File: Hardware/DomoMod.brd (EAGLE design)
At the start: 80 x 30 mm, 47 parts, among them Q1 BSS138, Q2 BSS138, T1 MMBT2222A, U1 NCS36000, U2 CCS811, U3 BME280, U4 PIR

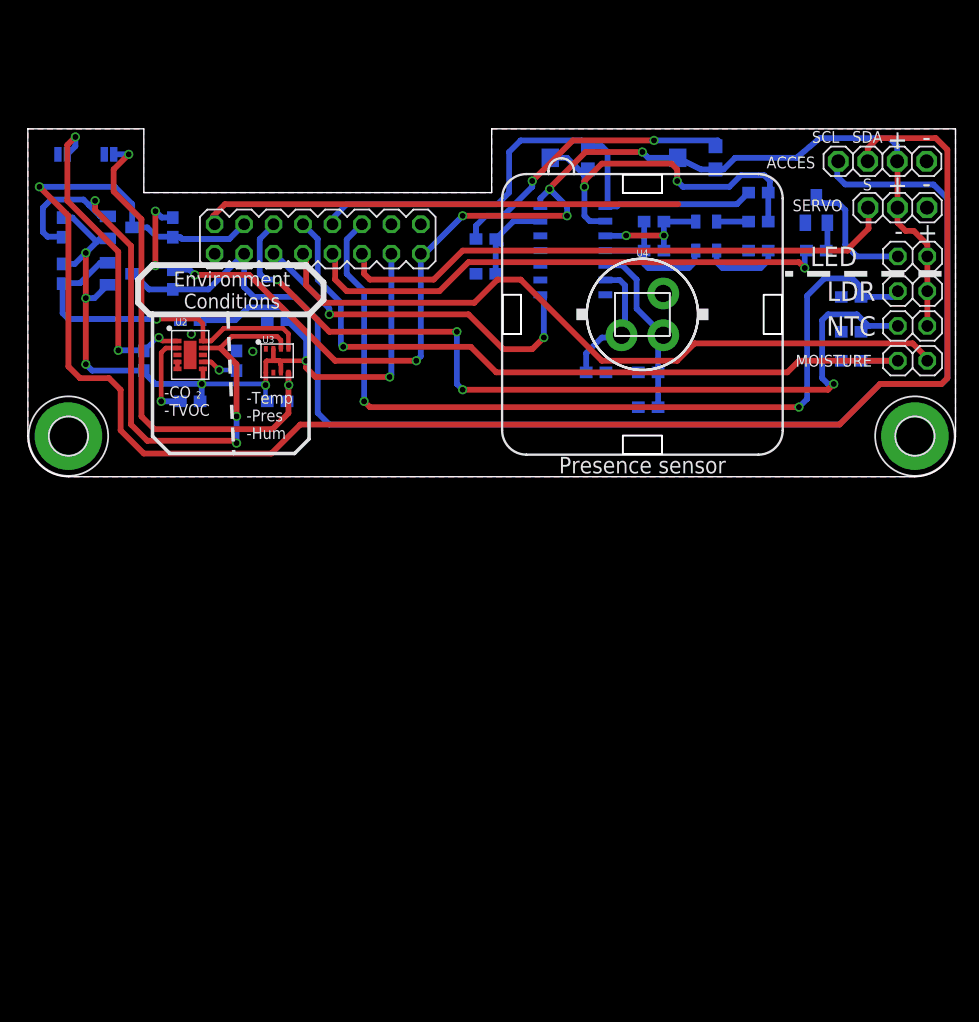
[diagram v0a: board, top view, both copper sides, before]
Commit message: Component replacement: NCS36000 -> BD9251FV
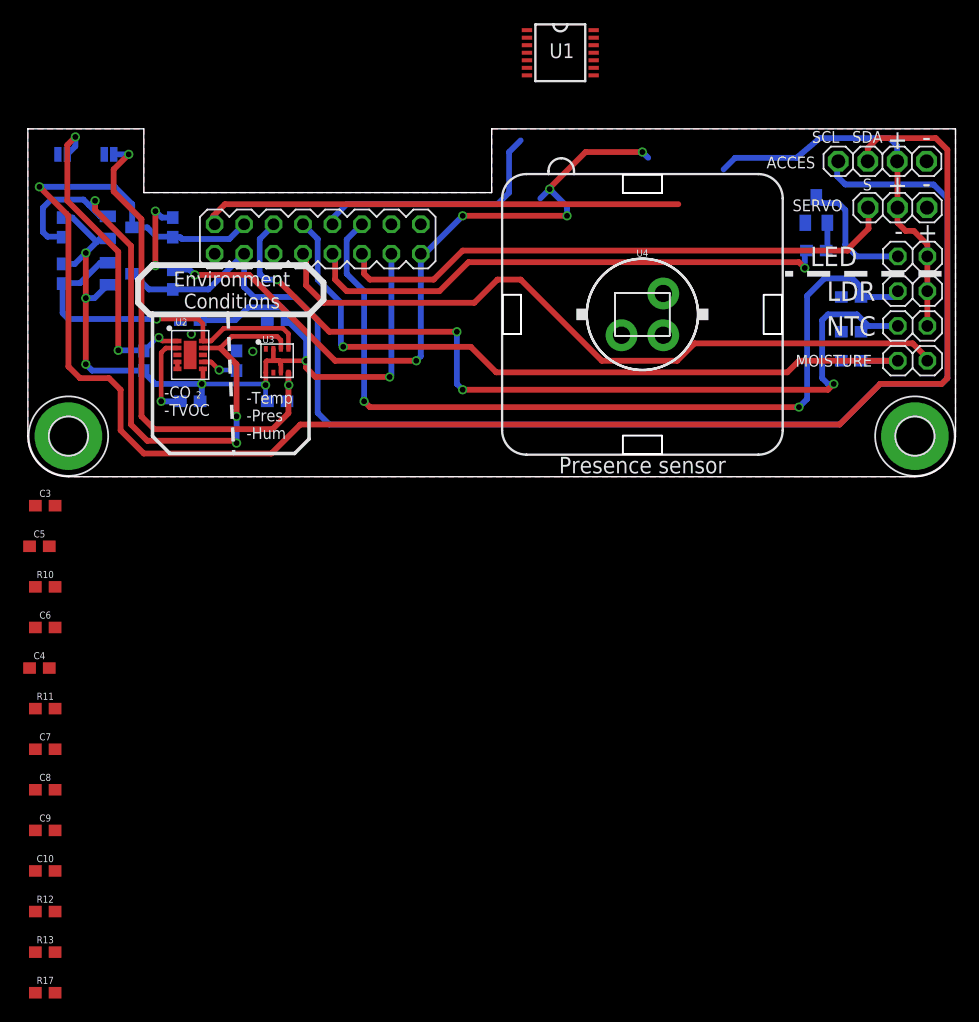
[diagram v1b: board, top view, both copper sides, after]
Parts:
- removed POT1, POT2: 1M, openPIR-temp:TRIMPOT-TC33X
- added C10: 10uF, SparkFun-Capacitors:0603
- C3: value 22uF -> 1.0uF; device SparkFun-Capacitors:0805 -> SparkFun-Capacitors:0603
- C4: value 10nF -> 1.0uF
- C5: value 0.1uF -> 1.0uF
- C6: value 0.1uF -> 6.9uF
- C7: value 22uF -> 15nF; device SparkFun-Capacitors:0805 -> SparkFun-Capacitors:0603
- C8: value 10nF -> 6.9uF
- C9: value 0.1uF -> 15nF
- R10: value 10k -> 47k
- R11: value 10k -> 4.7M
- R12: value 43k -> 47k
- R13: value 51k -> 4.7M; device openPIR-temp:0603 -> SparkFun-Resistors:0603
- R17: value 560k -> 220k; device openPIR-temp:0603 -> SparkFun-Resistors:0603
- U1: value NCS36000 -> BD9251FV; device openPIR-temp:SO14 -> SpaceDIY_IC:TSSOP-14
- moved R17 84.7 mm to (1.50, -44.5), flipped to the top, turned to 0 degrees
- moved C8 80.2 mm to (1.50, -27.0), flipped to the top
- moved R11 74.5 mm to (1.50, -20.0), flipped to the top, turned to 0 degrees
- moved C7 72.9 mm to (1.50, -23.5), flipped to the top, turned to 0 degrees
- moved R13 72.3 mm to (1.50, -41.0), flipped to the top
- moved R10 68.0 mm to (1.50, -9.50), flipped to the top, turned to 0 degrees
- moved R12 67.8 mm to (1.50, -37.5), flipped to the top, turned to 0 degrees
- moved C4 64.1 mm to (1.00, -16.5), flipped to the top, turned to 0 degrees
- moved C9 61.2 mm to (1.50, -30.5), flipped to the top
- moved C3 61.1 mm to (1.50, -2.50), flipped to the top, turned to 0 degrees
- moved C5 54.6 mm to (1.00, -6.00), flipped to the top
- moved C6 52.3 mm to (1.50, -13.0), flipped to the top, turned to 0 degrees
- moved U1 17.0 mm to (46.0, 36.5), flipped to the top, turned to 0 degrees
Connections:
- removed net N$11: POT2.1, R13.2
- removed net N$3: C3.2, R10.2
- removed net N$4: C7.2, R11.1
- removed net N$6: C4.2, C7.1, R17.2, U1.3
- removed net N$7: C8.1, POT1.2, POT1.3, R11.2, U1.2
- removed net N$8: C9.1, R13.1, U1.13
- new net A1N: C7.2, R10.1, R11.2, U1.5
- new net A1O: C7.1, C8.2, R11.1, U1.6
- new net A2N: C9.2, R12.1, R13.2, U1.8
- new net A2O: C10.1, C9.1, R13.1, U1.9
- new net A2P: C8.1, R12.2, U1.7
- new net COMP: C10.2, R17.2, U1.11
- new net OUT: U1.12
- new net REF: R17.1, U1.10
- net A2: no longer C8.2, POT1.1, U1.1
- net D8: no longer U1.8
- net GND: now also C3.2, C4.2, U1.1; no longer C9.2, R10.1, R12.1, U1.7
- net N$1: now also C6.1, R10.2; no longer C5.1, R12.2, U1.5, U4.S
- net N$2: now also C3.1, U1.4, U4.S; no longer C6.1, U1.6, U4.D
- net N$5: now also U1.3, U4.D; no longer C3.1, R17.1, U1.4
- net VCC: now also C5.1; no longer POT2.2, POT2.3
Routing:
- net N$7: track 32.4 -> 0.00 mm, vias 2 -> 0
- net D8: track 31.2 -> 0.00 mm, vias 2 -> 0
- net N$11: track 26.0 -> 0.00 mm, vias 2 -> 0
- net A2: track 47.1 -> 21.6 mm
- net N$1: track 15.3 -> 0.00 mm
- net N$5: track 12.7 -> 0.00 mm
- net N$2: track 11.7 -> 0.00 mm
- net N$6: track 10.3 -> 0.00 mm, vias 2 -> 0
- net N$8: track 8.14 -> 0.00 mm
- net VCC: track 110.7 -> 103.3 mm
- net N$3: track 6.78 -> 0.00 mm
- net N$4: track 2.75 -> 0.00 mm

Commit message: BRD and Production files updated for component BD9251FV
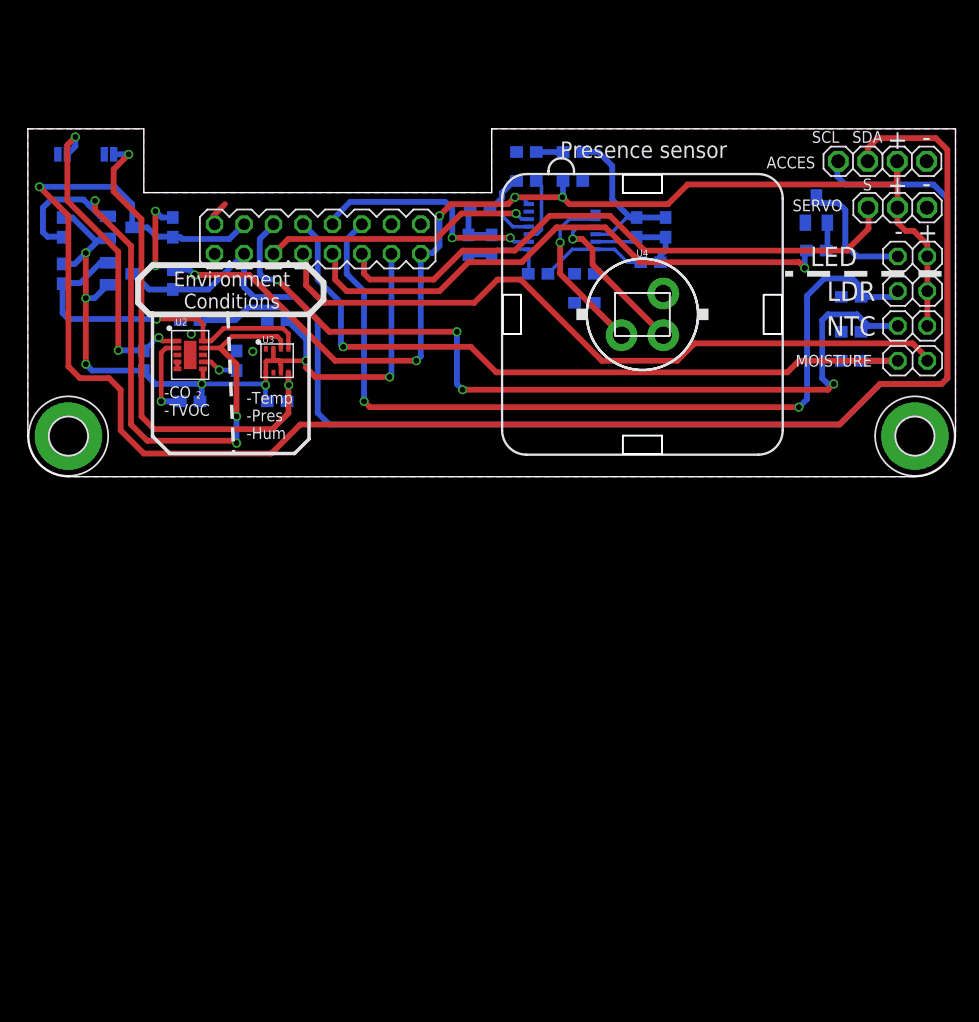
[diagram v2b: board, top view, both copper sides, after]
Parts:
- moved R17 81.4 mm to (43.0, 25.5), flipped to the bottom
- moved R13 71.1 mm to (38.0, 20.0), flipped to the bottom, turned to 270 degrees
- moved C7 69.9 mm to (55.0, 21.5), flipped to the bottom, turned to 90 degrees
- moved R12 69.5 mm to (44.0, 17.5), flipped to the bottom, turned to 180 degrees
- moved C8 69.2 mm to (53.7, 18.5), flipped to the bottom, turned to 180 degrees
- moved C10 68.2 mm to (39.0, 23.0), flipped to the bottom, turned to 180 degrees
- moved R11 65.8 mm to (52.5, 21.5), flipped to the bottom, turned to 90 degrees
- moved C9 63.5 mm to (40.0, 20.0), flipped to the bottom, turned to 270 degrees
- moved R10 59.0 mm to (47.0, 28.0), flipped to the bottom
- moved C6 58.3 mm to (43.0, 28.0), flipped to the bottom
- moved C4 56.6 mm to (48.0, 15.0), flipped to the bottom
- moved C5 55.8 mm to (47.0, 25.5), flipped to the bottom, turned to 180 degrees
- moved C3 50.6 mm to (48.0, 17.5), flipped to the bottom
- moved U1 15.0 mm to (46.0, 21.5), flipped to the bottom
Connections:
- removed net OUT: U1.12
- net A2: now also U1.9
- net A2O: no longer U1.9
- net D8: now also U1.12
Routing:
- net D0: track 41.3 -> 2.19 mm
- net D8: track 0.00 -> 23.7 mm, vias 0 -> 1
- net N$2: track 0.00 -> 22.9 mm, vias 0 -> 1
- net N$5: track 0.00 -> 18.6 mm, vias 0 -> 1
- net A1N: track 0.00 -> 14.9 mm
- net A2P: track 0.00 -> 9.33 mm
- net A1O: track 0.00 -> 8.54 mm
- net COMP: track 0.00 -> 7.55 mm
- net A2N: track 0.00 -> 7.53 mm
- net REF: track 0.00 -> 5.64 mm
- net VCC: track 103.3 -> 107.7 mm, vias 8 -> 7
- net A2O: track 0.00 -> 4.21 mm
- net D6: track 46.0 -> 48.5 mm
- net D5: track 49.3 -> 51.8 mm
- net N$1: track 0.00 -> 2.30 mm
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
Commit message: Added Schematics.pdf
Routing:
- net D0: track 2.19 -> 0.00 mm
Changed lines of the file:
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@@
 <signal name="D0">
 <contactref element="SV1" pad="2"/>
-<wire x1="17" y1="23.5" x2="16" y2="22.5" width="0.5" layer="1"/>
-<wire x1="16" y1="22.5" x2="16" y2="21.88" width="0.5" layer="1"/>
-<wire x1="16" y1="21.88" x2="16.11" y2="21.77" width="0.5" layer="1"/>
 </signal>
 <signal name="!RST">

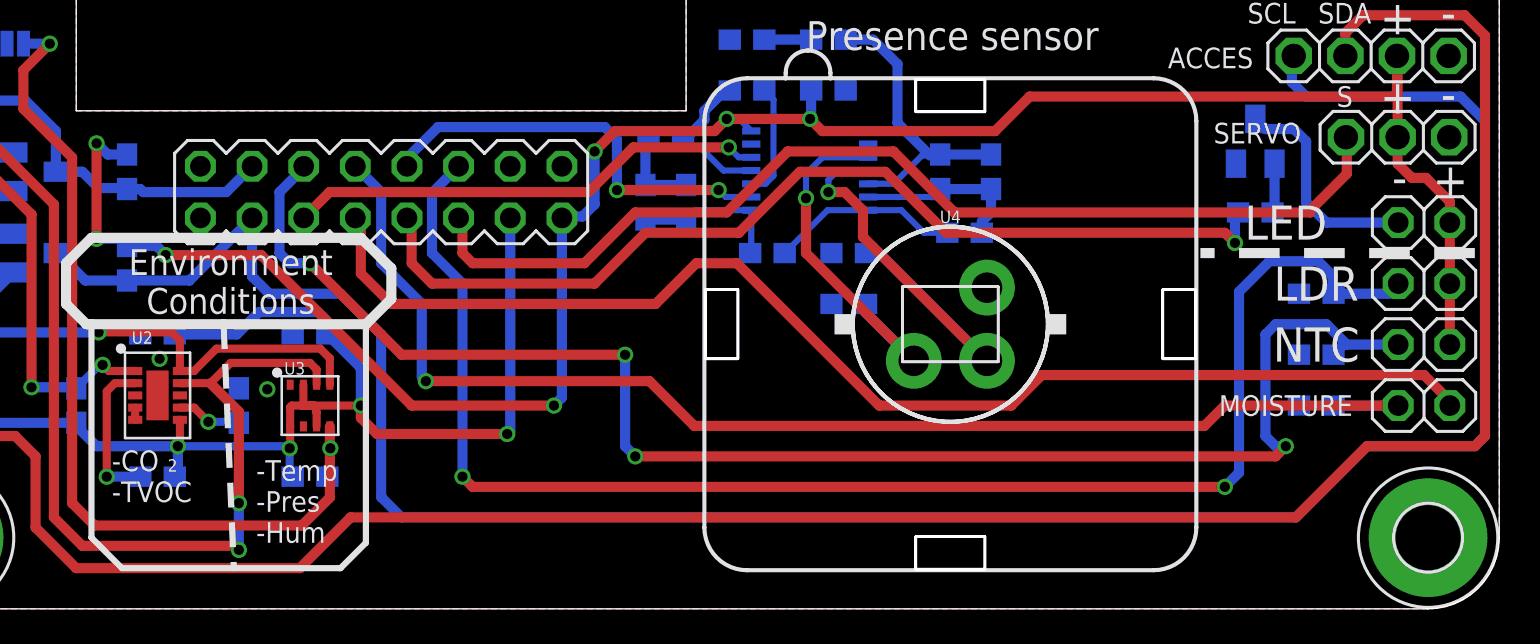
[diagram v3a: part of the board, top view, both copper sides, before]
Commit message: Fixed connector interface (rows were changed)
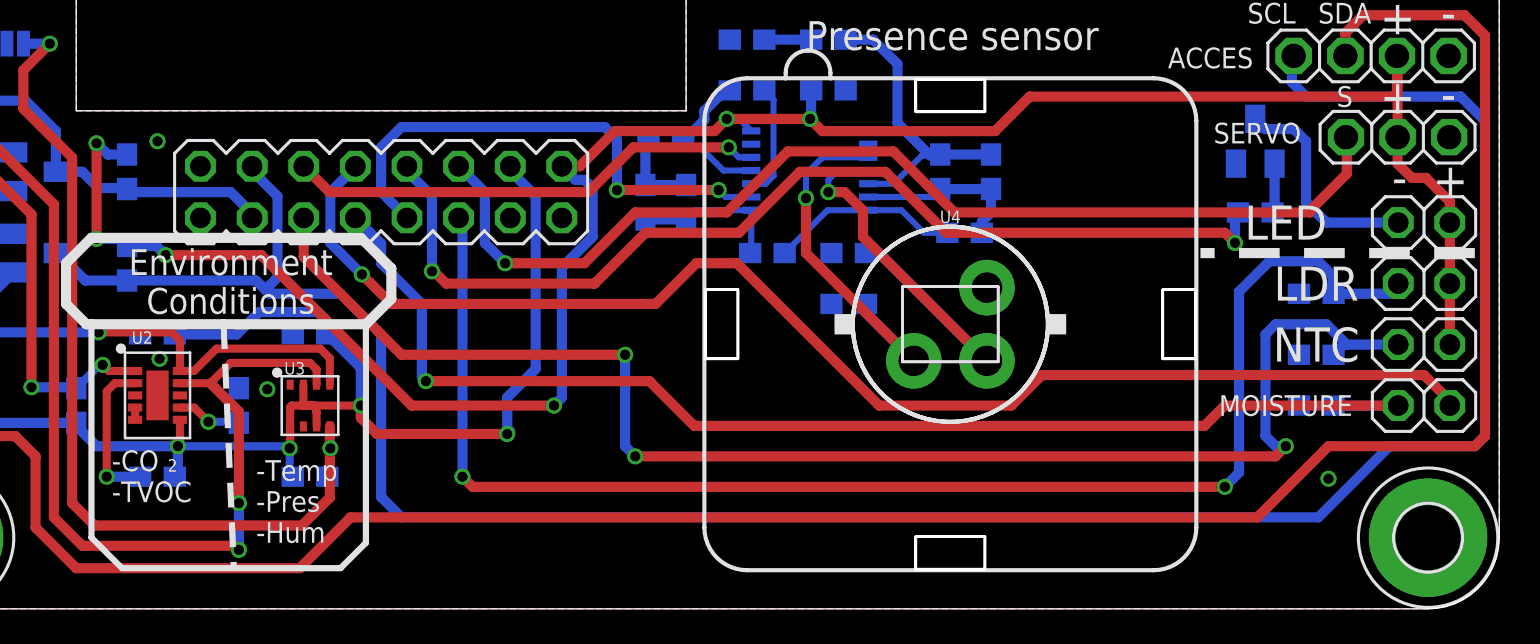
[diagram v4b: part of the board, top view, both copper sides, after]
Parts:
- renumbered SV1 to SV2
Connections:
- removed net D0: SV2.2
- removed net D1: SV2.1
- net 3.3V: now also SV2.14; no longer SV2.13
- net A1: now also SV2.11; no longer SV2.12
- net A2: now also SV2.9; no longer SV2.10
- net A3: now also SV2.7; no longer SV2.8
- net A4: now also SV2.5; no longer SV2.6
- net D2: now also SV2.3; no longer SV2.4
- net D3: now also SV2.4; no longer SV2.3
- net D5: now also SV2.12; no longer SV2.11
- net D6: now also SV2.10; no longer SV2.9
- net D7: now also SV2.8; no longer SV2.7
- net D8: now also SV2.6; no longer SV2.5
- net GND: now also SV2.13, SV2.15; no longer SV2.14, SV2.16
- net VCC: now also SV2.16; no longer SV2.15
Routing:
- net A2: track 20.9 -> 25.5 mm
- net A4: track 75.5 -> 71.4 mm, vias 4 -> 3
- net 3.3V: track 81.3 -> 85.1 mm
- net D7: track 62.1 -> 65.8 mm, vias 0 -> 1
- net A1: track 73.9 -> 70.2 mm
- net D3: track 113.3 -> 115.9 mm
- net A3: track 64.3 -> 61.8 mm
- net D6: track 48.5 -> 50.7 mm, vias 1 -> 2
- net D5: track 51.8 -> 53.4 mm, vias 0 -> 1
- net VCC: track 107.7 -> 109.2 mm, vias 7 -> 6

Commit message: Updated design files
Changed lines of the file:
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@@
 <signal name="D5">
 <wire x1="37.5" y1="19.5" x2="35" y2="17" width="0.5" layer="1"/>
-<wire x1="35" y1="17" x2="31.6" y2="17" width="0.5" layer="1"/>
+<wire x1="35" y1="17" x2="31.1" y2="17" width="0.5" layer="1"/>
 <wire x1="70.7" y1="19.5" x2="53.2" y2="19.5" width="0.5" layer="1"/>
 <wire x1="53.2" y1="19.5" x2="50.2" y2="22.5" width="0.5" layer="1"/>
@@
 <wire x1="30.1" y1="18" x2="31.1" y2="17" width="0.5" layer="16"/>
 <via x="31.1" y="17" extent="1-16" drill="0.5"/>
-<wire x1="31.1" y1="17" x2="31.6" y2="17" width="0.5" layer="1"/>
 </signal>
 <signal name="D6">
